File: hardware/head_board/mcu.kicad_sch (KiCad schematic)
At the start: 49 parts, among them SW1 BOOTSEL, U3 RP2040, U4 TVS, U5 W25Q128JVS, U9 74HC2G34, Y1 12MHz

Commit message: v1 revision to the schematic
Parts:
- removed C64: 100n, Capacitor_SMD:C_0402_1005Metric_Pad0.74x0.62mm_HandSolder, symbol Device:C_Small
- removed TP22: AUX, TestPoint:TestPoint_Pad_D1.0mm, symbol Connector:TestPoint_Small
- removed TP4: 3V3, TestPoint:TestPoint_Pad_D1.0mm, symbol Connector:TestPoint_Small
- removed TP5: RST, TestPoint:TestPoint_Pad_D1.0mm, symbol Connector:TestPoint_Small
- removed TP6: SWD, TestPoint:TestPoint_Pad_D1.0mm, symbol Connector:TestPoint_Small
- removed TP7: SWCLK, TestPoint:TestPoint_Pad_D1.0mm, symbol Connector:TestPoint_Small
- removed TP8: GND, TestPoint:TestPoint_Pad_D1.0mm, symbol Connector:TestPoint_Small
- removed U4: TVS, Package_TO_SOT_SMD:SOT-23-6, symbol Power_Protection:USBLC6-2SC6
- removed U9: 74HC2G34, Package_TO_SOT_SMD:SOT-363_SC-70-6, symbol winterbloom:74HC2G34
- added C?: 100n, Capacitor_SMD:C_0402_1005Metric_Pad0.74x0.62mm_HandSolder, symbol Device:C_Small
- added D?: ACT, winterbloom:LED_0805_Kingbright_APT2012, symbol Device:LED_Filled
- added J?: SWD, winterbloom:Connector_Cortex_Debug_IDC_2x05_P1.27mm_Vertical_Shrouded_SMD, symbol winterbloom:Conn_SWD
- added R?: 10K, Resistor_SMD:R_0402_1005Metric_Pad0.72x0.64mm_HandSolder, symbol Device:R_US
- added R?: 1k, Resistor_SMD:R_0603_1608Metric_Pad0.98x0.95mm_HandSolder, symbol Device:R_US
- added SW?: RESET, winterbloom:Tactile_Switch_4.2mm, symbol winterbloom:Tactile_Switch
- Y1: symbol Device:Crystal_GND24_Small -> winterbloom:Crystal_12MHz_4Pin
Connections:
- net CAM_LED_LV is gone; now on net CAM_LED: U3.15 (GPIO12)
- net USB_D+ is gone; now on net D+: R11.1
- net USB_D- is gone; now on net D-: R12.1
- net +3V3: now also J?.1 (VCC), R?.2
- net GND: now also C?.2, J?.3 (GND), J?.5 (GND), J?.9 (GNDDetect), R?.2, SW?.2
- net QSPI_CS: now also R?.1
- net RUN: now also C?.1, J?.10 (~{RESET}), SW?.1
- net SWCLK: now also J?.4 (SWCLK)
- net SWD: now also J?.2 (SWDIO)
- net XIN: now also Y1.1; no longer Y1.3
- net at C10.1, R9.2: now also Y1.3; no longer Y1.1
- net QWIIC_SCL: now reaches U3.17 (GPIO14)
- net QWIIC_SDA: now reaches U3.18 (GPIO15)
- net ACT_LED: now reaches U3.41 (GPIO29_ADC3)
- net ACT_LED: now also D?.2 (A)
- net AUX_LV renamed AUX_OUT
- new net: D?.1 (K), R?.1
- no-connect marks 14 -> 12
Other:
- note added: "* Flash ~{CS} pullup may not be necessary depending on flash chip"
- note added: "* Make sure C16 is close to pin 44 (VREG_IN) * Make sure C17 is close to pin 45 (VREG_OUT) * Make sure R11 & R12 are close to pins 46 & 47 (USB D- & D+)"
- note added: "* Verify R9, C9, and C10 values with actual crystal"
- note added: "12 MHz crystal"
- note added: "Debug, reset, and boot select"
- note added: "Microcontroller"
- note added: "Power supply bypassing"
- note added: "QSPI flash"
- note added: "Schematic notes: * 1kΩ resistor on TMC UART TX per TMC2209 datasheet Figure 4.1 * ACT_LED can be re-assigned to any free pin * Check RP2040 pin mux before re-assigning UART & I2C pins * Crystal requires extra start up time"
- note removed: "1K on TX per TMC2209 Datasheet Figure 4.1"
- note removed: "Make sure C16 is close to pin 44"
- note removed: "Make sure C17 is close to pin 45"
- note removed: "Make sure R11 & R12 are close to pins 46 & 47"
- note removed: "Place close to connector"
- company: (none) -> Winterbloom
- title: (none) -> Candela Head
- moved on the sheet: C10, C11, C12, C13, C14, C15, C16, C17, C18, C19, C20, C21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

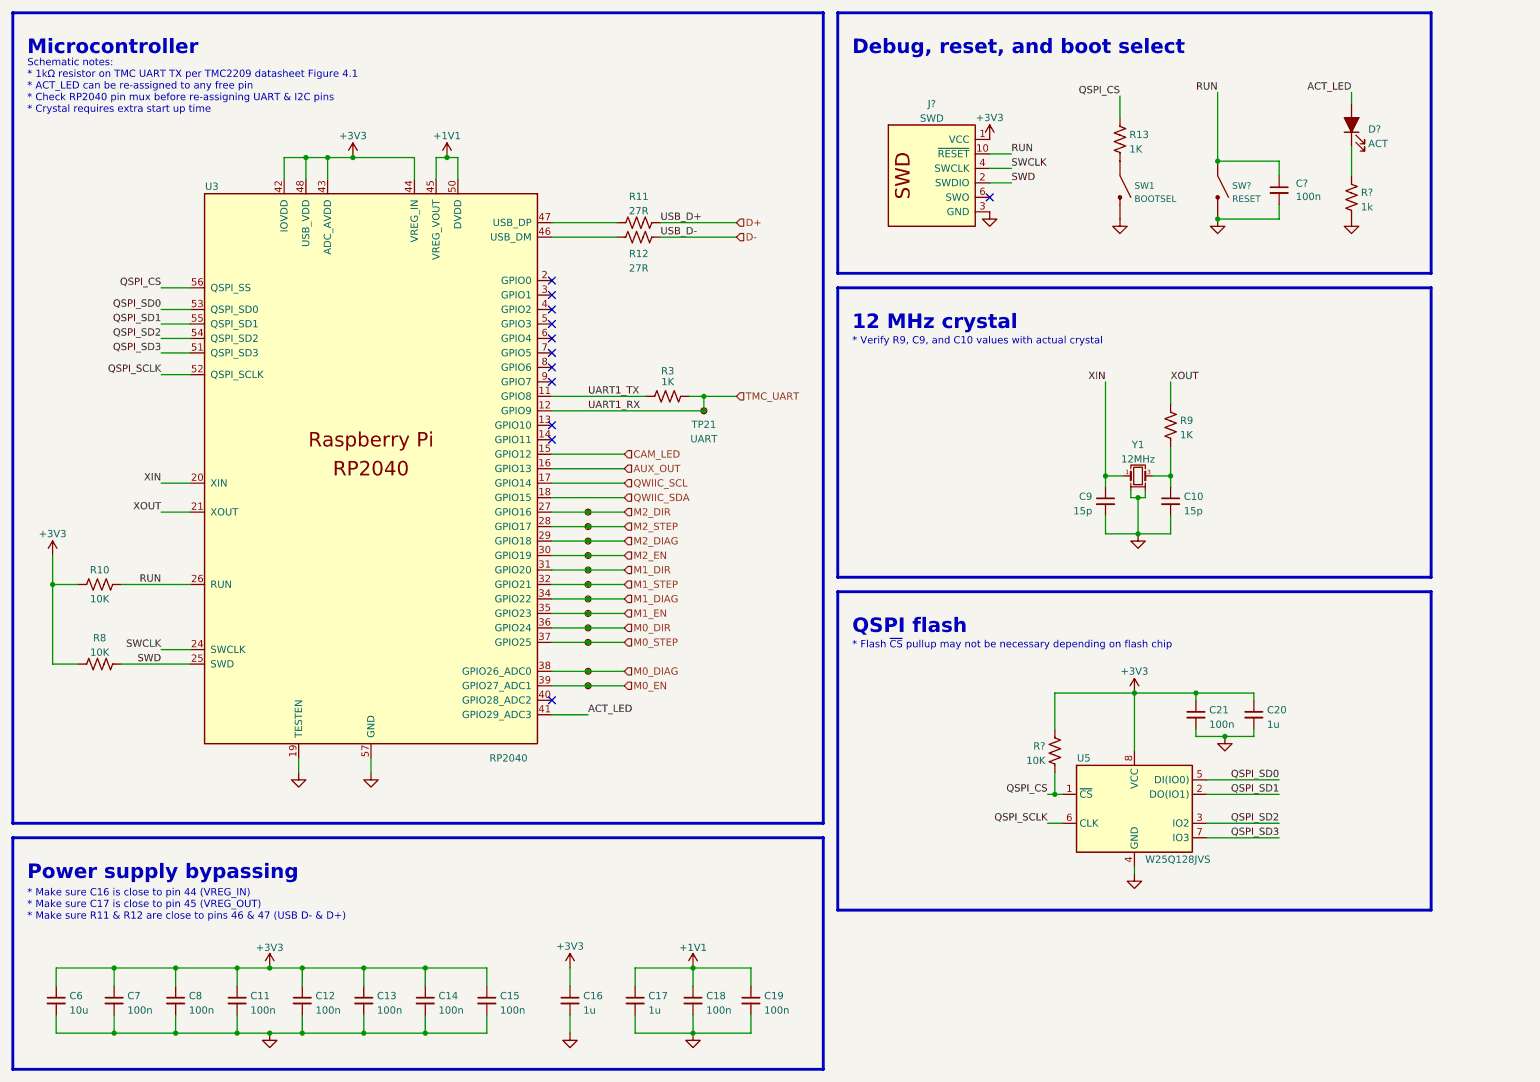
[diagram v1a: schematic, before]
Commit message: Footprints assigned
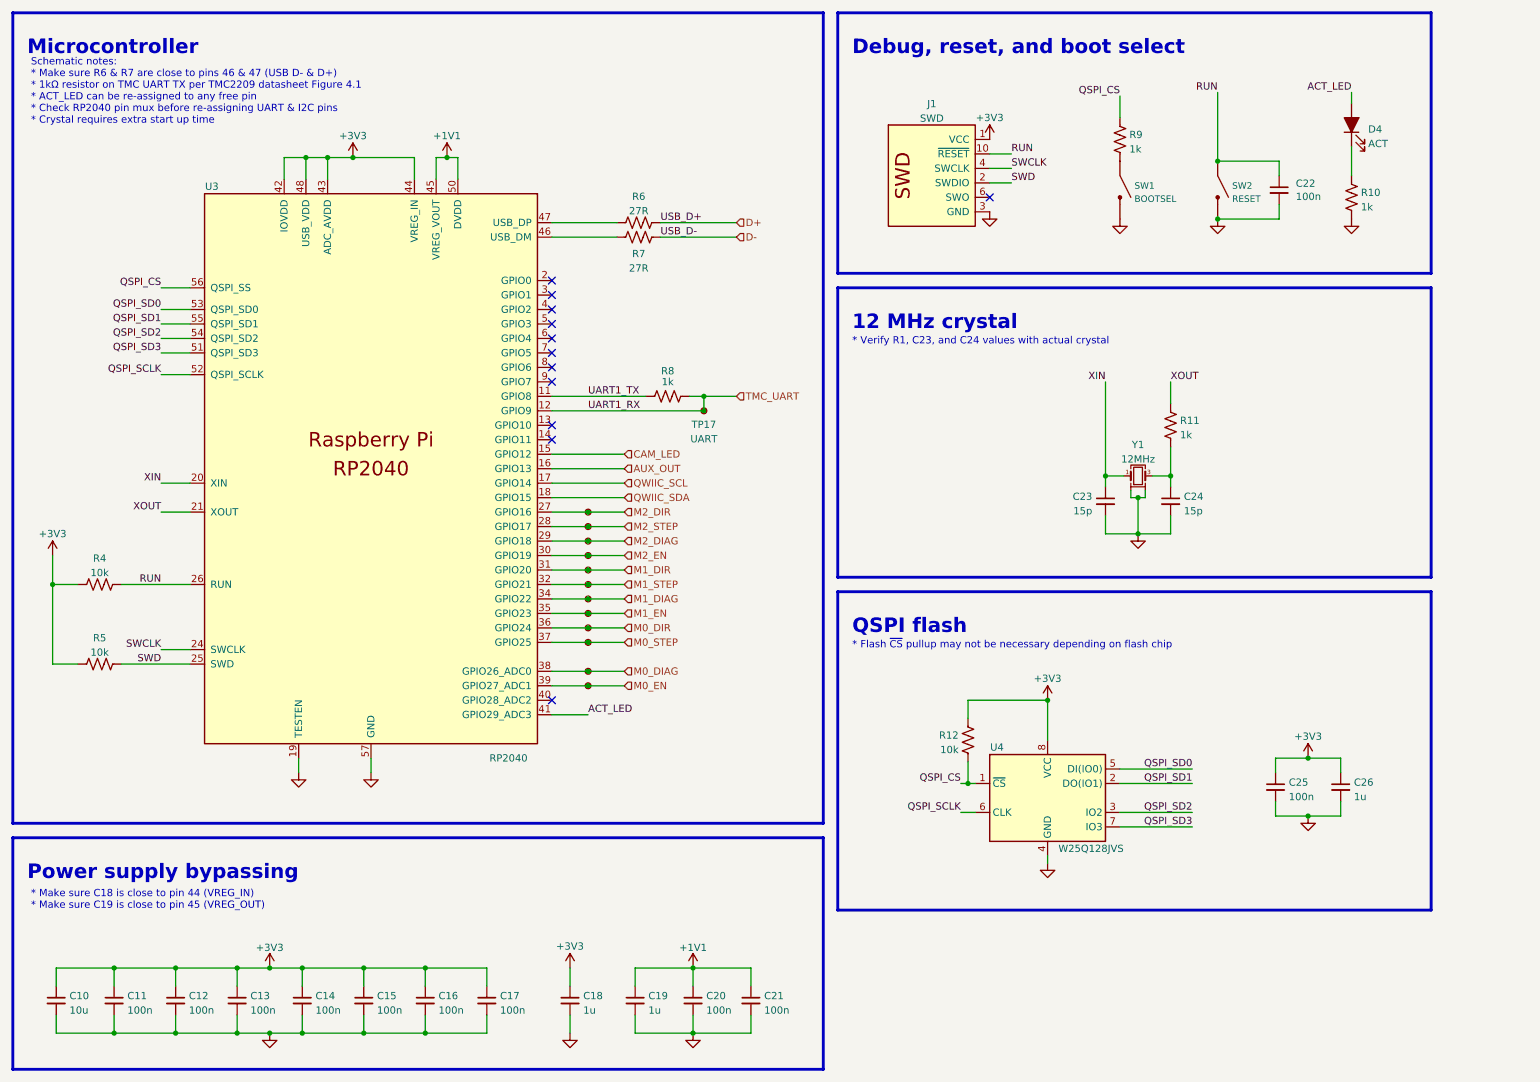
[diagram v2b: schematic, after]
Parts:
- C10: renamed from C6; Rating (none) -> 6.3V
- C11: renamed from C7; Rating 16V -> 6.3V
- C12: renamed from C8; Rating 16V -> 6.3V
- C13: renamed from C11; Rating 16V -> 6.3V
- C14: renamed from C12; Rating 16V -> 6.3V
- C15: renamed from C13; Rating 16V -> 6.3V
- C16: renamed from C14; Rating 16V -> 6.3V
- C17: renamed from C15; Rating 16V -> 6.3V
- C18: renamed from C16; Rating 10V -> 6.3V
- C19: renamed from C17; Rating 10V -> 6.3V
- C20: renamed from C18; Rating 16V -> 6.3V
- C21: renamed from C19; Rating 16V -> 6.3V
- C22: renamed from C?; Rating 16V -> 6.3V
- C23: renamed from C9; Rating 5% 50V -> 5% 10V
- C24: renamed from C10; Rating 5% 50V -> 5% 10V
- C25: renamed from C21; Rating 16V -> 6.3V
- C26: renamed from C20; Rating (none) -> 6.3V
- D4: renamed from D?; Rating (none) -> Red
- R10: renamed from R?; Rating (none) -> 200mW
- R11: renamed from R9; value 1K -> 1k; Rating (none) -> 63mW
- R12: renamed from R?; value 10K -> 10k; Rating (none) -> 63mW
- R4: renamed from R10; value 10K -> 10k; Rating (none) -> 63mW
- R5: renamed from R8; value 10K -> 10k; Rating (none) -> 63mW
- R6: renamed from R11; Rating (none) -> 63mW
- R7: renamed from R12; Rating (none) -> 63mW
- R8: renamed from R3; value 1K -> 1k; Rating (none) -> 63mW
- R9: renamed from R13; value 1K -> 1k; Rating (none) -> 63mW
- gave numbers to parts that had none: 2
- renumbered TP14 to TP10, TP15 to TP11, TP16 to TP12, TP17 to TP13, TP18 to TP14, TP19 to TP15, TP20 to TP16, TP21 to TP17, TP9 to TP5, TP10 to TP6, TP11 to TP7, TP12 to TP8, TP13 to TP9, U5 to U4
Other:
- note added: "* Make sure C18 is close to pin 44 (VREG_IN) * Make sure C19 is close to pin 45 (VREG_OUT)"
- note added: "* Verify R1, C23, and C24 values with actual crystal"
- note added: "Schematic notes: * Make sure R6 & R7 are close to pins 46 & 47 (USB D- & D+) * 1kΩ resistor on TMC UART TX per TMC2209 datasheet Figure 4.1 * ACT_LED can be re-assigned to any free pin * Check RP2040 pin mux before re-assigning UART & I2C pins * Crystal requires extra start up time"
- note removed: "* Make sure C16 is close to pin 44 (VREG_IN) * Make sure C17 is close to pin 45 (VREG_OUT) * Make sure R11 & R12 are close to pins 46 & 47 (USB D- & D+)"
- note removed: "* Verify R9, C9, and C10 values with actual crystal"
- note removed: "Schematic notes: * 1kΩ resistor on TMC UART TX per TMC2209 datasheet Figure 4.1 * ACT_LED can be re-assigned to any free pin * Check RP2040 pin mux before re-assigning UART & I2C pins * Crystal requires extra start up time"
- moved on the sheet: C25, C26, R12, U4

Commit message: Finish up layout for v1, ended up removing some stuff
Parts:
- removed C22: 100n, Capacitor_SMD:C_0402_1005Metric_Pad0.74x0.62mm_HandSolder, symbol Device:C_Small
- removed J1: SWD, winterbloom:Connector_Cortex_Debug_IDC_2x05_P1.27mm_Vertical_Shrouded_SMD, symbol winterbloom:Conn_SWD
- removed SW2: RESET, winterbloom:Tactile_Switch_4.2mm, symbol winterbloom:Tactile_Switch
- removed TP10: M1STP, TestPoint:TestPoint_Pad_D1.0mm, symbol Connector:TestPoint_Small
- removed TP11: M1DAG, TestPoint:TestPoint_Pad_D1.0mm, symbol Connector:TestPoint_Small
- removed TP12: M1EN, TestPoint:TestPoint_Pad_D1.0mm, symbol Connector:TestPoint_Small
- removed TP13: M0DIR, TestPoint:TestPoint_Pad_D1.0mm, symbol Connector:TestPoint_Small
- removed TP14: M0STP, TestPoint:TestPoint_Pad_D1.0mm, symbol Connector:TestPoint_Small
- removed TP15: M0DAG, TestPoint:TestPoint_Pad_D1.0mm, symbol Connector:TestPoint_Small
- removed TP16: M0EN, TestPoint:TestPoint_Pad_D1.0mm, symbol Connector:TestPoint_Small
- removed TP5: M2DIR, TestPoint:TestPoint_Pad_D1.0mm, symbol Connector:TestPoint_Small
- removed TP6: M2STP, TestPoint:TestPoint_Pad_D1.0mm, symbol Connector:TestPoint_Small
- removed TP7: M2DAG, TestPoint:TestPoint_Pad_D1.0mm, symbol Connector:TestPoint_Small
- removed TP8: M2EN, TestPoint:TestPoint_Pad_D1.0mm, symbol Connector:TestPoint_Small
- removed TP9: M1DIR, TestPoint:TestPoint_Pad_D1.0mm, symbol Connector:TestPoint_Small
- added TP5: GND, TestPoint:TestPoint_Pad_D1.0mm, symbol Connector:TestPoint
- added TP6: 3V3, TestPoint:TestPoint_Pad_D1.0mm, symbol Connector:TestPoint
- added TP7: ~{RST}, TestPoint:TestPoint_Pad_D1.0mm, symbol Connector:TestPoint
- added TP8: SWD, TestPoint:TestPoint_Pad_D1.0mm, symbol Connector:TestPoint
- added TP9: SWC, TestPoint:TestPoint_Pad_D1.0mm, symbol Connector:TestPoint
- C10: mpn (none) -> CL32B106KBJNNNE
- R10: mpn AC0603FR-075K1L -> (none)
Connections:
- net +3V3: now also TP6.1
- net ACT_LED: now also U3.18 (GPIO15); no longer U3.41 (GPIO29_ADC3)
- net AUX_OUT: now also U3.3 (GPIO1); no longer U3.16 (GPIO13)
- net CAM_LED: now also U3.2 (GPIO0); no longer U3.15 (GPIO12)
- net GND: now also TP5.1
- net M0_DIAG: now also U3.31 (GPIO20); no longer U3.38 (GPIO26_ADC0)
- net M0_DIR: now also U3.29 (GPIO18); no longer U3.36 (GPIO24)
- net M0_EN: now also U3.32 (GPIO21); no longer U3.39 (GPIO27_ADC1)
- net M0_STEP: now also U3.30 (GPIO19); no longer U3.37 (GPIO25)
- net M1_DIAG: now also U3.36 (GPIO24); no longer U3.34 (GPIO22)
- net M1_DIR: now also U3.34 (GPIO22); no longer U3.31 (GPIO20)
- net M1_EN: now also U3.37 (GPIO25); no longer U3.35 (GPIO23)
- net M1_STEP: now also U3.35 (GPIO23); no longer U3.32 (GPIO21)
- net M2_DIAG: now also U3.40 (GPIO28_ADC2); no longer U3.29 (GPIO18)
- net M2_DIR: now also U3.38 (GPIO26_ADC0); no longer U3.27 (GPIO16)
- net M2_EN: now also U3.41 (GPIO29_ADC3); no longer U3.30 (GPIO19)
- net M2_STEP: now also U3.39 (GPIO27_ADC1); no longer U3.28 (GPIO17)
- net QWIIC_SCL: no longer U3.17 (GPIO14)
- net QWIIC_SDA: no longer U3.18 (GPIO15)
- net RUN: now also TP7.1
- net SWCLK: now also TP9.1
- net SWD: now also TP8.1
- net TMC_UART: now also U3.28 (GPIO17); no longer U3.12 (GPIO9)
- net UART1_TX: now also U3.27 (GPIO16); no longer U3.11 (GPIO8)
- no-connect marks 12 -> 11
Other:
- note added: "Debug, boot select, and LED"
- note removed: "Debug, reset, and boot select"
- moved on the sheet: R8, R9, SW1, TP17

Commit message: V2 of the head board (Jellyfish)
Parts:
- added D1: AUX, winterbloom:LED_0805_Kingbright_APT2012, symbol Device:LED_Filled
- added R28: 1k, Resistor_SMD:R_0603_1608Metric_Pad0.98x0.95mm_HandSolder, symbol Device:R_US
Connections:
- net GND: now also R28.2
- net QWIIC_SCL: now also U3.14 (GPIO11)
- net QWIIC_SDA: now also U3.13 (GPIO10)
- net AUX_LED: now reaches U3.16 (GPIO13)
- net AUX_LED: now also D1.2 (A)
- net IN_1: now reaches U3.4 (GPIO2)
- net IN_2: now reaches U3.5 (GPIO3)
- net BLTOUCH_CONTROL: now reaches U3.6 (GPIO4)
- net BLTOUCH_STATUS: now reaches U3.7 (GPIO5)
- new net: D1.1 (K), R28.1
- no-connect marks 11 -> 6
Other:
- title: Candela Head -> Jellyfish
- moved on the sheet: D4, R10, R9, SW1, TP5, TP6, TP7, TP8, TP9
